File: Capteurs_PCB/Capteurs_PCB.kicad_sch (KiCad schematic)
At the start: 21 parts, among them J1 Conn_01x04, J101 Conn_01x03, J103 Conn_02x20_Odd_Even, J104 Conn_ST_STDC14, J2 Conn_01x03, J4 Conn_01x02, J6 Conn_01x03, J7 Conn_01x03, U1 STM32L412KBTx

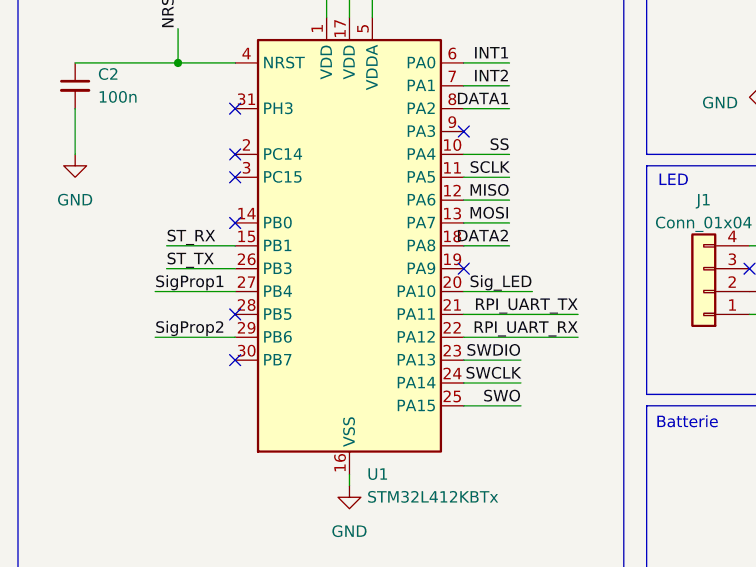
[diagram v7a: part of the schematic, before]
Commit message: Avancement PCB mais encore des problèmes
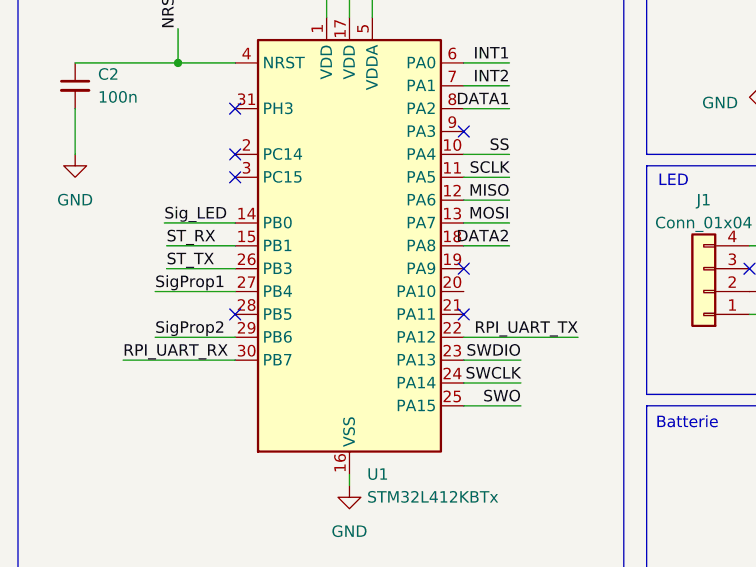
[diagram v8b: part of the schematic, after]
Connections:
- net RPI_UART_RX: now also U1.30 (PB7); no longer U1.22 (PA12)
- net RPI_UART_TX: now also U1.22 (PA12); no longer U1.21 (PA11)
- net Sig_LED: now also U1.14 (PB0); no longer U1.20 (PA10)
- no-connect marks 39 -> 38
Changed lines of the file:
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@@
   (no_connect (at 110.49 52.07))
   (no_connect (at 97.79 29.21))
-  (no_connect (at 36.83 88.9))
+  (no_connect (at 62.23 99.06))
   (no_connect (at 97.79 31.75))
   (no_connect (at 97.79 67.31))
   (no_connect (at 110.49 46.99))
   (no_connect (at 36.83 99.06))
-  (no_connect (at 36.83 104.14))
   (no_connect (at 110.49 44.45))
   (no_connect (at 110.49 39.37))
@@
     (stroke (width 0) (type default))
   )
-  (wire (pts (xy 62.23 96.52) (xy 69.85 96.52))
-    (stroke (width 0) (type default))
-  )
   (wire (pts (xy 143.51 62.23) (xy 144.78 62.23))
     (stroke (width 0) (type default))
@@
     (stroke (width 0) (type default))
   )
+  (wire (pts (xy 24.384 104.14) (xy 36.83 104.14))
+    (stroke (width 0) (type default))
+  )
   (wire (pts (xy 114.3 90.17) (xy 119.38 90.17))
     (stroke (width 0) (type default))
@@
     (stroke (width 0) (type default))
   )
-  (wire (pts (xy 74.93 99.06) (xy 62.23 99.06))
-    (stroke (width 0) (type default))
-  )
   (wire (pts (xy 110.49 67.31) (xy 111.76 67.31))
     (stroke (width 0) (type default))
@@
   )
   (wire (pts (xy 114.3 95.25) (xy 119.38 95.25))
+    (stroke (width 0) (type default))
+  )
+  (wire (pts (xy 28.956 88.9) (xy 36.83 88.9))
     (stroke (width 0) (type default))
   )
@@
     (effects (font (size 1.27 1.27)) (justify right bottom))
   )
-  (label "RPI_UART_RX" (at 74.93 101.6 180) (fields_autoplaced)
+  (label "RPI_UART_TX" (at 74.93 101.6 180) (fields_autoplaced)
     (effects (font (size 1.27 1.27)) (justify right bottom))
   )
@@
     (effects (font (size 1.27 1.27)) (justify right bottom))
   )
-  (label "RPI_UART_TX" (at 74.93 99.06 180) (fields_autoplaced)
-    (effects (font (size 1.27 1.27)) (justify right bottom))
+  (label "RPI_UART_RX" (at 24.384 104.14 0) (fields_autoplaced)
+    (effects (font (size 1.27 1.27)) (justify left bottom))
   )
   (label "RPI_UART_RX" (at 125.73 36.83 180) (fields_autoplaced)
@@
     (effects (font (size 1.27 1.27)) (justify left bottom))
   )
-  (label "Sig_LED" (at 69.85 96.52 180) (fields_autoplaced)
-    (effects (font (size 1.27 1.27)) (justify right bottom))
+  (label "Sig_LED" (at 28.956 88.9 0) (fields_autoplaced)
+    (effects (font (size 1.27 1.27)) (justify left bottom))
   )
   (symbol (lib_id "Connector_Generic:Conn_01x03") (at 219.71 74.93 180) (unit 1)
